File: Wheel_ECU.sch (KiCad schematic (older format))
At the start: 19 parts, among them J1 Conn_01x04, J2 Conn_01x04, J3 Conn_01x02, J4 Debug, U1 IFX9201SG, U2 TLE4964, U3 XMC1404_F064, U4 TLE7251

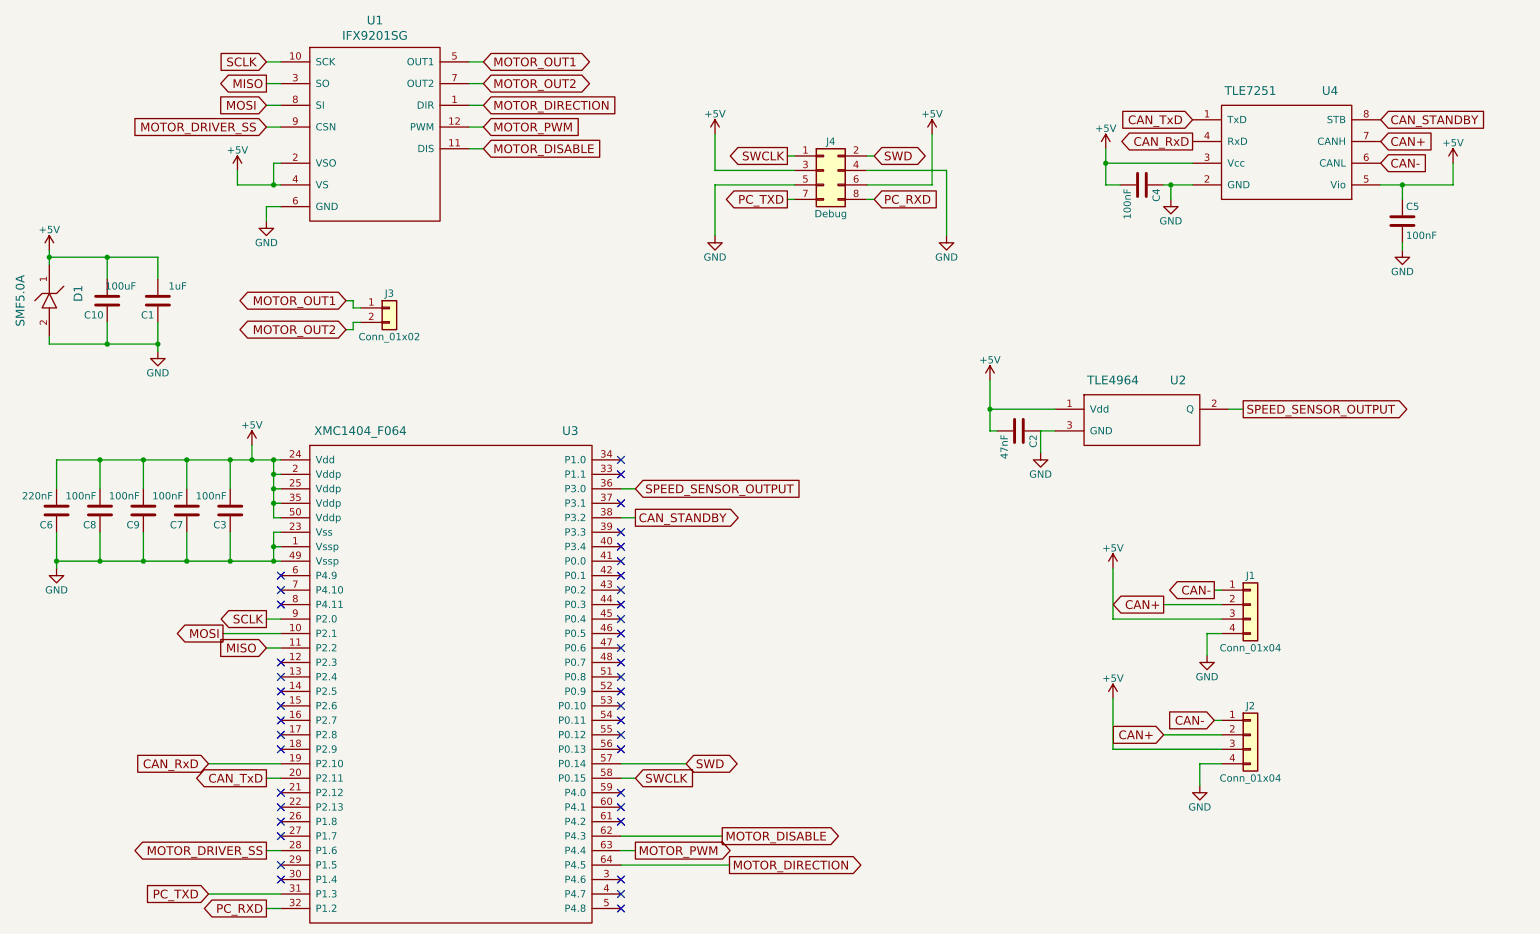
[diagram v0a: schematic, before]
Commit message: Supply the motor directly from the battery
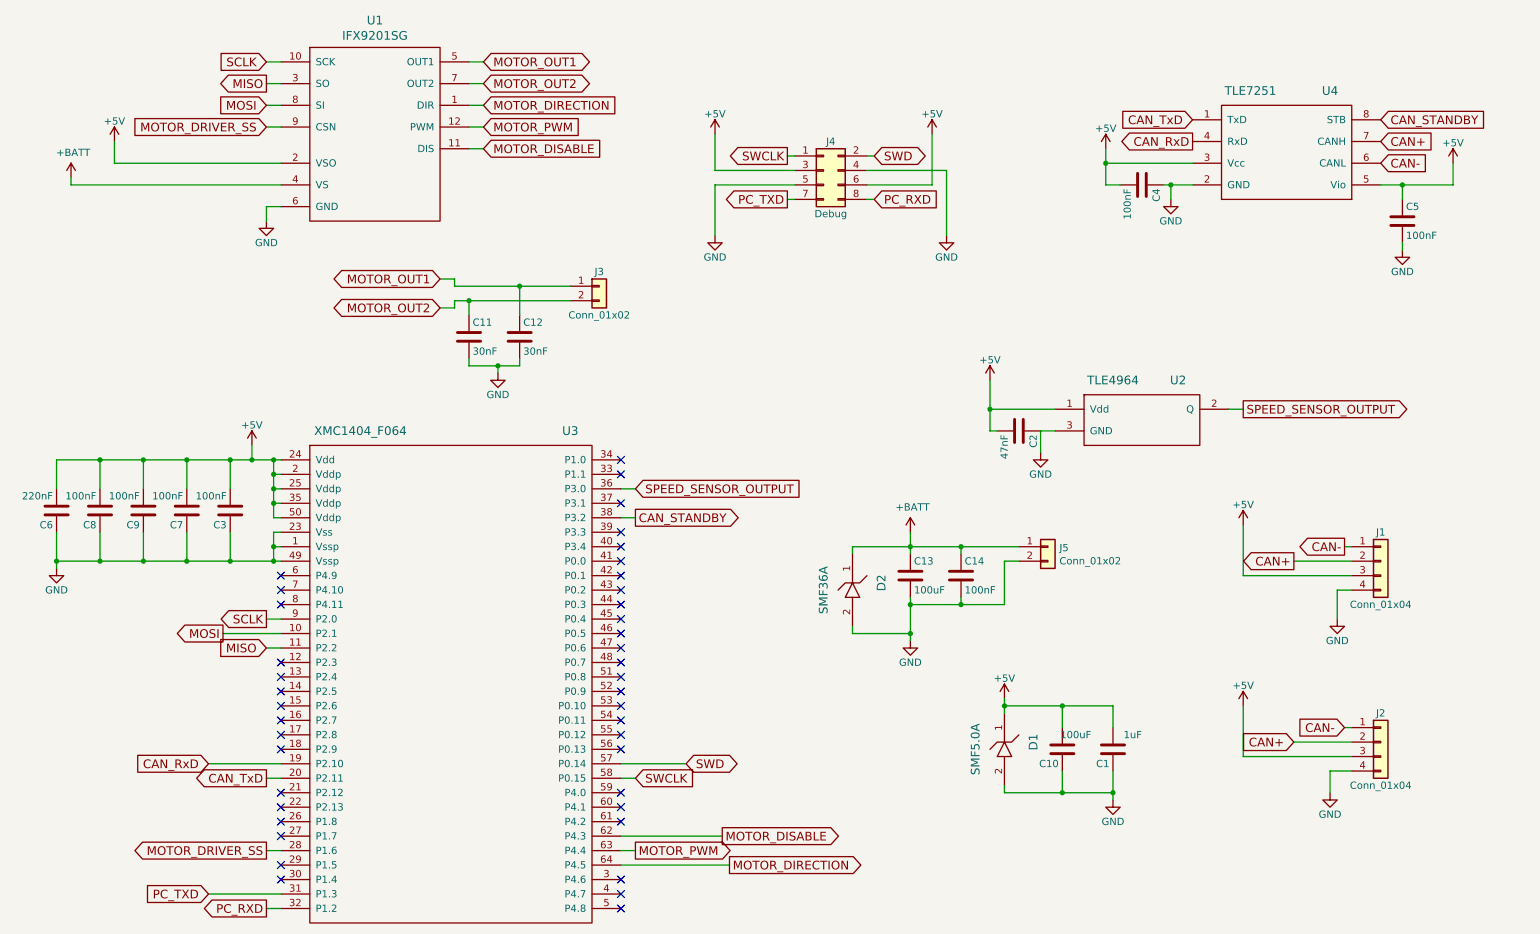
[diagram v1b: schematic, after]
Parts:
- added C11, C12: 30nF, WheelECU:C_0805_HandSoldering, symbol Wheel_ECU-rescue:C
- added C13: 100uF, WheelECU:C_0805_HandSoldering, symbol Wheel_ECU-rescue:C
- added C14: 100nF, WheelECU:C_0805_HandSoldering, symbol Wheel_ECU-rescue:C
- added D2: SMF36A, Diode_SMD:D_SOD-123F, symbol Wheel_ECU-rescue:TVS_Diode
- added J5: Conn_01x02, Connector_PinHeader_2.54mm:PinHeader_1x02_P2.54mm_Vertical, symbol Connector_Generic:Conn_01x02
- D1: footprint Diodes_SMD:D_MELF -> Diode_SMD:D_SOD-123F
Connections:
- net +5V: no longer U1.4 (VS)
- net GND: now also C11.2, C12.2, C13.2, C14.2, D2.2, J5.2 (Pin_2)
- net MOTOR_OUT1: now also C12.1
- net MOTOR_OUT2: now also C11.1
- new net +BATT: C13.1, C14.1, D2.1, J5.1 (Pin_1), U1.4 (VS)
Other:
- moved on the sheet: C1, C10, D1, J1, J2, J3

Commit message: Improve the placement of the motor driver and connector
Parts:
- J3: footprint Pin_Headers:Pin_Header_Straight_2x01_Pitch2.54mm_SMD -> Connector_PinHeader_2.54mm:PinHeader_1x02_P2.54mm_Vertical
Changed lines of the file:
@@
 F 0 "J3" H 4700 2600 50  0000 C CNN
 F 1 "Conn_01x02" H 4700 2300 50  0000 C CNN
-F 2 "Pin_Headers:Pin_Header_Straight_2x01_Pitch2.54mm_SMD" H 4700 2500 50  0001 C CNN
+F 2 "Connector_PinHeader_2.54mm:PinHeader_1x02_P2.54mm_Vertical" H 4700 2500 50  0001 C CNN
 F 3 "" H 4700 2500 50  0001 C CNN
 	1    4700 2500

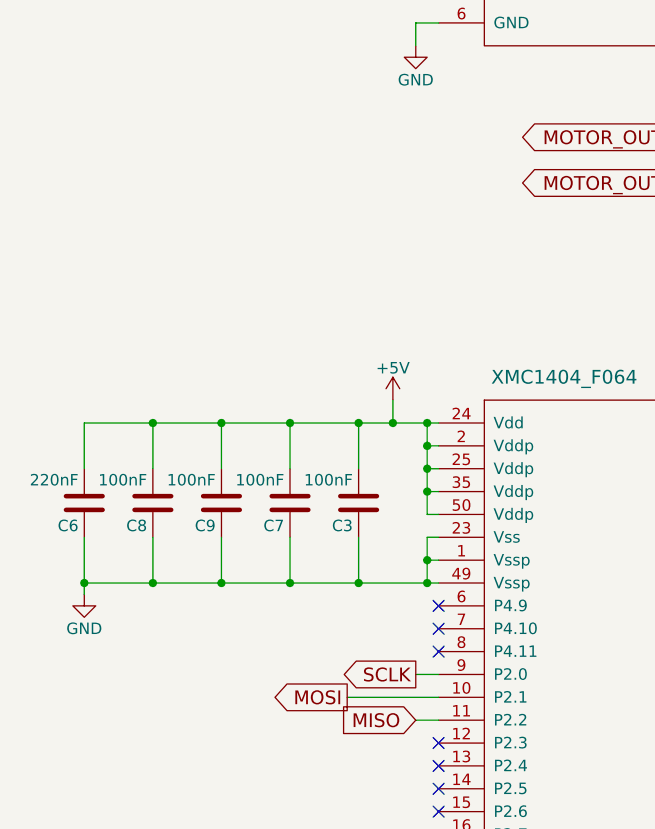
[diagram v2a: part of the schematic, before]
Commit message: Add status LED
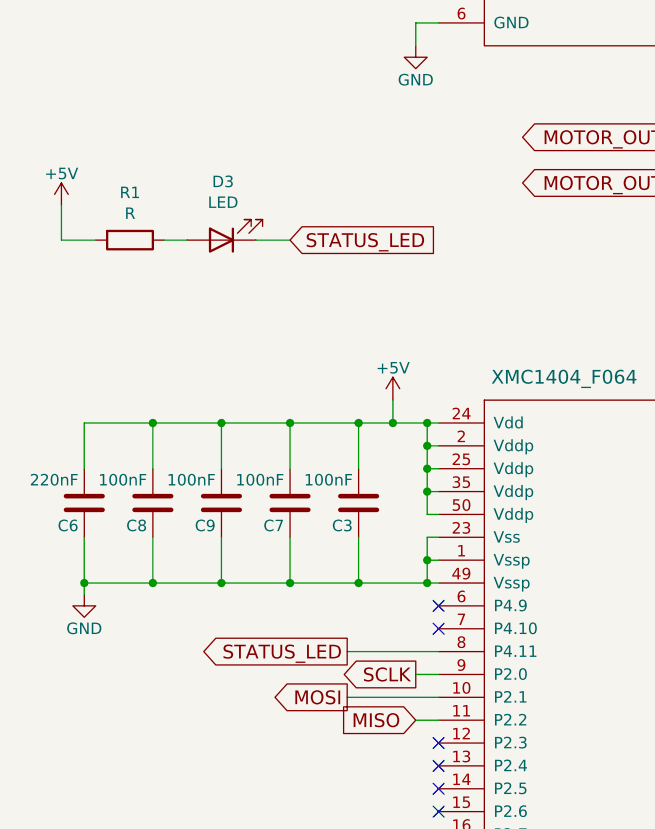
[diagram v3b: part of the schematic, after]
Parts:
- added D3: LED, WheelECU:C_0805_HandSoldering, symbol Device:LED
- added R1: R, WheelECU:C_0805_HandSoldering, symbol Device:R
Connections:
- net +5V: now also R1.2
- net STATUS_LED: now reaches U3.8 (P4.11)
- net STATUS_LED: now also D3.1 (K)
- new net: D3.2 (A), R1.1
- no-connect marks 41 -> 40
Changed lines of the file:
@@
 NoConn ~ 2500 4500
 NoConn ~ 2500 4600
-NoConn ~ 2500 4700
 NoConn ~ 2500 5100
 NoConn ~ 2500 5200
@@
 Wire Wire Line
 	6850 4900 6850 4700
+$Comp
+L Wheel_ECU-rescue:+5V #PWR025
+U 1 1 6034D88D
+P 850 2750
+F 0 "#PWR025" H 850 2600 50  0001 C CNN
+F 1 "+5V" H 850 2890 50  0000 C CNN
+F 2 "" H 850 2750 50  0001 C CNN
+F 3 "" H 850 2750 50  0001 C CNN
+	1    850  2750
+	1    0    0    -1
+$EndComp
+$Comp
+L Device:LED D3
+U 1 1 6034E48A
+P 1550 2900
+F 0 "D3" H 1543 2645 50  0000 C CNN
+F 1 "LED" H 1543 2736 50  0000 C CNN
+F 2 "WheelECU:C_0805_HandSoldering" H 1550 2900 50  0001 C CNN
+F 3 "~" H 1550 2900 50  0001 C CNN
+	1    1550 2900
+	-1   0    0    1
+$EndComp
+$Comp
+L Device:R R1
+U 1 1 6035C8A5
+P 1150 2900
+F 0 "R1" V 943 2900 50  0000 C CNN
+F 1 "R" V 1034 2900 50  0000 C CNN
+F 2 "WheelECU:C_0805_HandSoldering" V 1080 2900 50  0001 C CNN
+F 3 "~" H 1150 2900 50  0001 C CNN
+	1    1150 2900
+	0    1    1    0
+$EndComp
+Wire Wire Line
+	850  2750 850  2900
+Wire Wire Line
+	850  2900 1000 2900
+Wire Wire Line
+	1300 2900 1400 2900
+Text GLabel 1850 2900 2    60   Input ~ 0
+STATUS_LED
+Wire Wire Line
+	1700 2900 1850 2900
+Text GLabel 2100 4700 0    60   Output ~ 0
+STATUS_LED
+Wire Wire Line
+	2500 4700 2100 4700
 $EndSCHEMATC

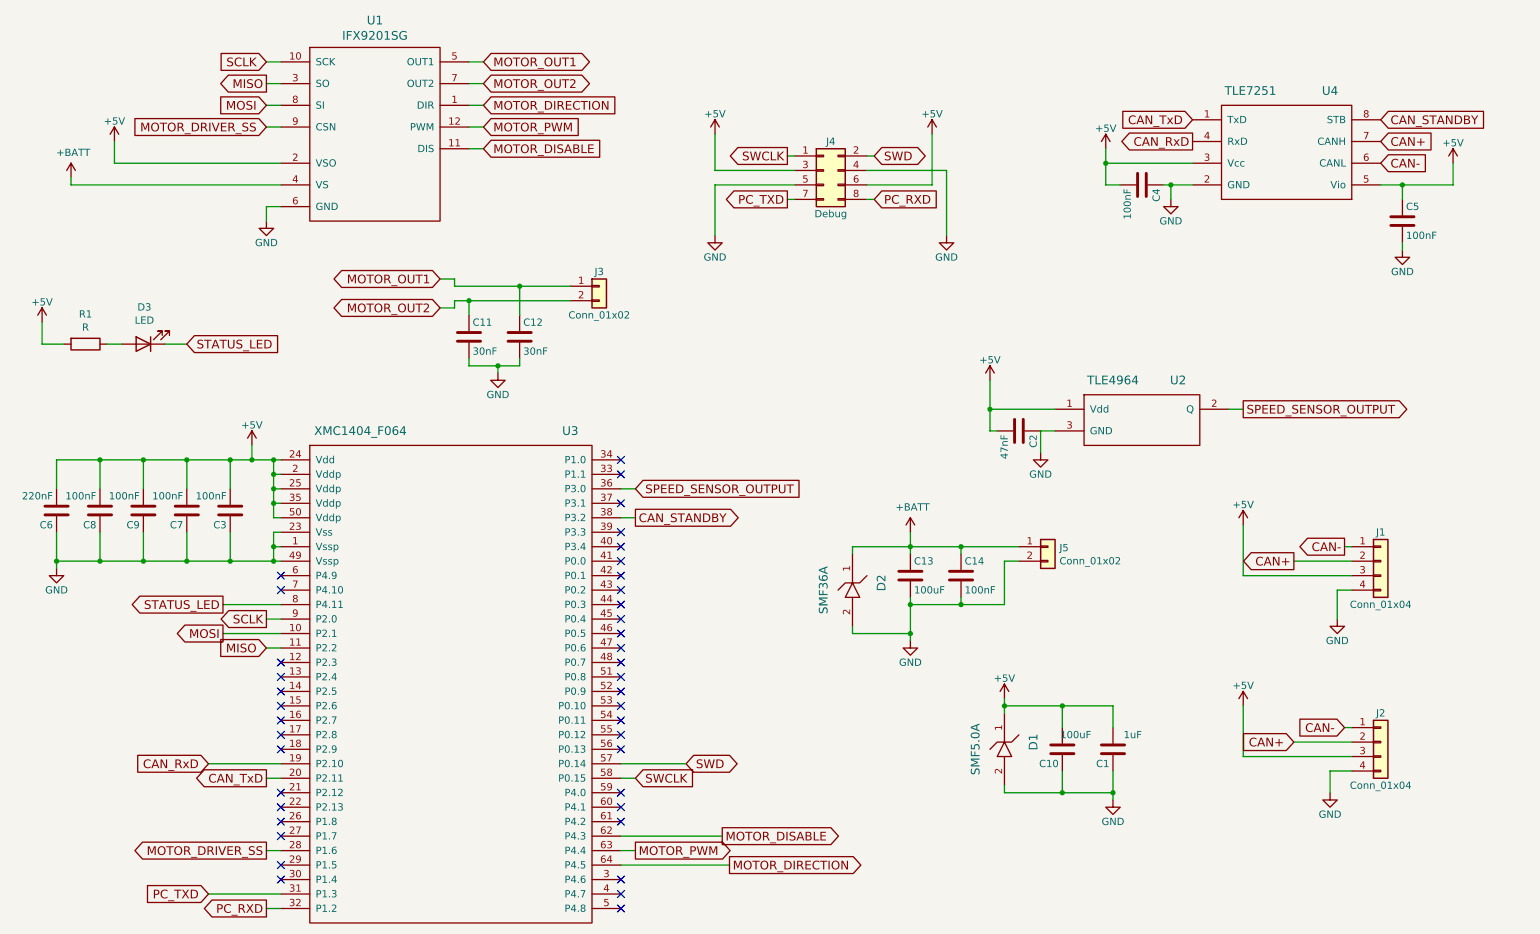
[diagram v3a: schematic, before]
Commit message: Add a temperature sensor (LM35D)
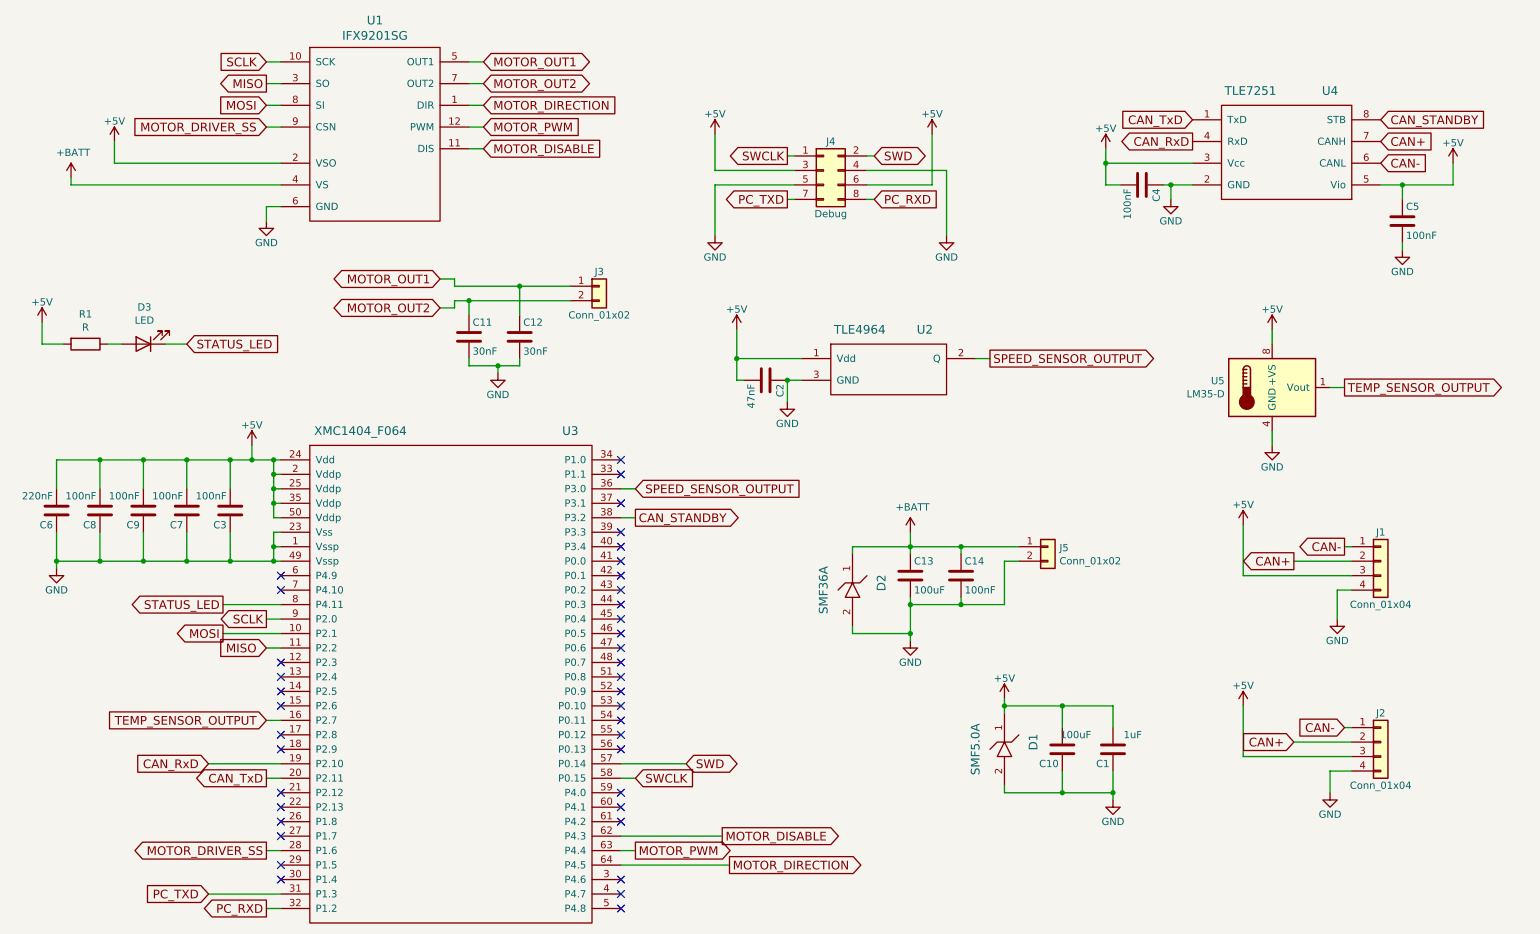
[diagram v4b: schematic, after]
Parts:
- added U5: LM35-D, Package_SO:SOIC-8_3.9x4.9mm_P1.27mm, symbol Sensor_Temperature:LM35-D
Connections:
- net +5V: now also U5.8 (+VS)
- net GND: now also U5.4 (GND)
- net TEMP_SENSOR_OUTPUT: now reaches U3.16 (P2.7)
- net TEMP_SENSOR_OUTPUT: now also U5.1 (Vout)
- no-connect marks 40 -> 39
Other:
- moved on the sheet: C2, U2
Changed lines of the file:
@@
 L Wheel_ECU-rescue:TLE4964 U2
 U 1 1 5BFAD6F2
-P 8500 3050
-F 0 "U2" H 8700 2950 60  0000 C CNN
-F 1 "TLE4964" H 8250 2950 60  0000 C CNN
-F 2 "TO_SOT_Packages_SMD:TSOT-23_HandSoldering" H 8500 3050 60  0001 C CNN
-F 3 "" H 8500 3050 60  0001 C CNN
-	1    8500 3050
+P 6750 2700
+F 0 "U2" H 6950 2600 60  0000 C CNN
+F 1 "TLE4964" H 6500 2600 60  0000 C CNN
+F 2 "TO_SOT_Packages_SMD:TSOT-23_HandSoldering" H 6750 2700 60  0001 C CNN
+F 3 "" H 6750 2700 60  0001 C CNN
+	1    6750 2700
 	1    0    0    -1
 $EndComp
@@
 L Wheel_ECU-rescue:C C2
 U 1 1 5BFADA57
-P 7600 3500
-F 0 "C2" H 7625 3600 50  0000 L CNN
-F 1 "47nF" H 7625 3400 50  0000 L CNN
-F 2 "Capacitors_SMD:C_0805_HandSoldering" H 7638 3350 50  0001 C CNN
-F 3 "" H 7600 3500 50  0001 C CNN
-	1    7600 3500
+P 5850 3150
+F 0 "C2" H 5875 3250 50  0000 L CNN
+F 1 "47nF" H 5875 3050 50  0000 L CNN
+F 2 "Capacitors_SMD:C_0805_HandSoldering" H 5888 3000 50  0001 C CNN
+F 3 "" H 5850 3150 50  0001 C CNN
+	1    5850 3150
 	0    1    1    0
 $EndComp
@@
 L Wheel_ECU-rescue:GND #PWR08
 U 1 1 5BFC30F3
-P 7750 3650
-F 0 "#PWR08" H 7750 3400 50  0001 C CNN
-F 1 "GND" H 7750 3500 50  0000 C CNN
-F 2 "" H 7750 3650 50  0001 C CNN
-F 3 "" H 7750 3650 50  0001 C CNN
-	1    7750 3650
+P 6000 3300
+F 0 "#PWR08" H 6000 3050 50  0001 C CNN
+F 1 "GND" H 6000 3150 50  0000 C CNN
+F 2 "" H 6000 3300 50  0001 C CNN
+F 3 "" H 6000 3300 50  0001 C CNN
+	1    6000 3300
 	1    0    0    -1
 $EndComp
@@
 L Wheel_ECU-rescue:+5V #PWR010
 U 1 1 5BFC3169
-P 7400 3150
-F 0 "#PWR010" H 7400 3000 50  0001 C CNN
-F 1 "+5V" H 7400 3290 50  0000 C CNN
-F 2 "" H 7400 3150 50  0001 C CNN
-F 3 "" H 7400 3150 50  0001 C CNN
-	1    7400 3150
+P 5650 2800
+F 0 "#PWR010" H 5650 2650 50  0001 C CNN
+F 1 "+5V" H 5650 2940 50  0000 C CNN
+F 2 "" H 5650 2800 50  0001 C CNN
+F 3 "" H 5650 2800 50  0001 C CNN
+	1    5650 2800
 	1    0    0    -1
 $EndComp
@@
 $EndComp
 Wire Wire Line
-	7850 3500 7750 3500
-Wire Wire Line
-	7750 3500 7750 3650
-Wire Wire Line
-	7400 3500 7450 3500
-Wire Wire Line
-	7400 3150 7400 3350
-Wire Wire Line
-	7850 3350 7400 3350
-Connection ~ 7400 3350
-Text GLabel 9150 3350 2    60   Output ~ 0
+	6100 3150 6000 3150
+Wire Wire Line
+	6000 3150 6000 3300
+Wire Wire Line
+	5650 3150 5700 3150
+Wire Wire Line
+	5650 2800 5650 3000
+Wire Wire Line
+	6100 3000 5650 3000
+Connection ~ 5650 3000
+Text GLabel 7400 3000 2    60   Output ~ 0
 SPEED_SENSOR_OUTPUT
 Wire Wire Line
-	9050 3350 9150 3350
+	7300 3000 7400 3000
 $Comp
 L Wheel_ECU-rescue:Conn_01x04 J1
@@
 NoConn ~ 2500 5300
 NoConn ~ 2500 5400
-NoConn ~ 2500 5500
 NoConn ~ 2500 5600
 NoConn ~ 2500 6000
@@
 NoConn ~ 2500 5700
 Wire Wire Line
-	7400 3350 7400 3500
+	5650 3000 5650 3150
 Wire Wire Line
 	8200 1650 8200 1800
@@
 Wire Wire Line
 	2500 4700 2100 4700
+$Comp
+L Sensor_Temperature:LM35-D U5
+U 1 1 6039ED20
+P 9350 3200
+F 0 "U5" H 9021 3246 50  0000 R CNN
+F 1 "LM35-D" H 9021 3155 50  0000 R CNN
+F 2 "Package_SO:SOIC-8_3.9x4.9mm_P1.27mm" H 9350 2800 50  0001 C CNN
+F 3 "http://www.ti.com/lit/ds/symlink/lm35.pdf" H 9350 3200 50  0001 C CNN
+	1    9350 3200
+	1    0    0    -1
+$EndComp
+Connection ~ 6000 3150
+$Comp
+L Wheel_ECU-rescue:GND #PWR027
+U 1 1 603AB356
+P 9350 3600
+F 0 "#PWR027" H 9350 3350 50  0001 C CNN
+F 1 "GND" H 9350 3450 50  0000 C CNN
+F 2 "" H 9350 3600 50  0001 C CNN
+F 3 "" H 9350 3600 50  0001 C CNN
+	1    9350 3600
+	1    0    0    -1
+$EndComp
+$Comp
+L Wheel_ECU-rescue:+5V #PWR026
+U 1 1 603AB7F6
+P 9350 2800
+F 0 "#PWR026" H 9350 2650 50  0001 C CNN
+F 1 "+5V" H 9350 2940 50  0000 C CNN
+F 2 "" H 9350 2800 50  0001 C CNN
+F 3 "" H 9350 2800 50  0001 C CNN
+	1    9350 2800
+	1    0    0    -1
+$EndComp
+Wire Wire Line
+	9350 2800 9350 2900
+Wire Wire Line
+	9350 3500 9350 3600
+Text GLabel 9850 3200 2    60   Output ~ 0
+TEMP_SENSOR_OUTPUT
+Wire Wire Line
+	9750 3200 9850 3200
+Text GLabel 2400 5500 0    60   Input ~ 0
+TEMP_SENSOR_OUTPUT
+Wire Wire Line
+	2500 5500 2400 5500
 $EndSCHEMATC
